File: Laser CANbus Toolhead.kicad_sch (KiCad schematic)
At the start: 79 parts, among them J101 In, J102 Laser, Q101 AO4407A, Q102 2N7002H, U101 STM32F072CBUx, U102 MP2459, U103 XC6206P332MR-G, U104 74AHCT1G125, U105 SN65HVD230, U106 ADXL343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

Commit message: feat: Major hardware upgrade to Rev. 1
- Replace MOSFET with CJAC70P06 (60V voltage rating)
- Upgrade sensor from ADXL345 to ICM-20602 (better availability, 6-axis IMU)
- Change Micro Fit 3.0 connectors from SMD to THT mounting
- Add connector pinouts to silkscreen for easier assembly
- Clean up component placement and optimize layout
- Update overview image to reflect current design
- Add component order numbers to BOM
- Update production files with current components
- Add comprehensive changelog and table of contents
- Improve documentation structure with language links
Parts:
- removed Q101: AO4407A, Package_SO:SOIC-8_3.9x4.9mm_P1.27mm, symbol Transistor_FET:FDS9435A
- removed U106: ADXL343, Package_LGA:LGA-14_3x5mm_P0.8mm_LayoutBorder1x6y, symbol Sensor_Motion:ADXL343
- added C124: 10u, Capacitor_SMD:C_0805_2012Metric, symbol Device:C
- added Q103: CJAC70P06, Package_DFN_QFN:AO_DFN-8-1EP_5.55x5.2mm_P1.27mm_EP4.12x4.6mm, symbol Transistor_FET:AON6411
- added U107: ICM-20602, Package_LGA:LGA-16_3x3mm_P0.5mm_LayoutBorder3x5y, symbol Sensor_Motion:ICM-20602
- C101, C102, C115: LCSC Part # (none) -> C1562; Manufacturer Part # (none) -> 0402CG330J500NT
- C103: value 4u7 -> 10u; footprint Capacitor_SMD:C_0402_1005Metric -> Capacitor_SMD:C_0805_2012Metric; LCSC Part # (none) -> C440198; Manufacturer Part # (none) -> GRM21BR61H106KE43L
- C104: value 4u7 -> 100n; LCSC Part # (none) -> C307331; Manufacturer Part # (none) -> CL05B104KB54PNC
- C105, C106, C107, C108, C109, C111, C113, C114, C117, C118, C120, C122, C123: LCSC Part # (none) -> C307331; Manufacturer Part # (none) -> CL05B104KB54PNC
- C110: value 10uF -> 10u
- C112: value 22uF -> 22u
- C119: LCSC Part # (none) -> C1538; Manufacturer Part # (none) -> 0402B472K500NT
- D103: LCSC Part # (none) -> C343993; Manufacturer Part # (none) -> PESD1CAN
- D104, D105, D106, D107: LCSC Part # (none) -> C2297; Manufacturer Part # (none) -> KT-0805G
- D108: LCSC Part # (none) -> C2296; Manufacturer Part # (none) -> KT-0805Y
- D109, D110: LCSC Part # (none) -> C2286; Manufacturer Part # (none) -> KT-0603R
- J101: footprint Connector_Molex:Molex_Micro-Fit_3.0_43045-0415_2x02_P3.00mm_Vertical -> Connector_Molex:Molex_Micro-Fit_3.0_43045-0412_2x02_P3.00mm_Vertical; FT Rotation Offset (none) -> 180; LCSC Part # (none) -> C492540; Manufacturer Part # (none) -> M3025V-2x2P
- J102: footprint Connector_Molex:Molex_Micro-Fit_3.0_43650-0321_1x03_P3.00mm_Vertical -> Connector_Molex:Molex_Micro-Fit_3.0_43650-0315_1x03_P3.00mm_Vertical; FT Rotation Offset (none) -> 180; LCSC Part # (none) -> C705183; Manufacturer Part # (none) -> M3025V-1x3P
- Q102: value 2N7002H -> 2N7002; LCSC Part # (none) -> C8545; Manufacturer Part # (none) -> 2N7002
- R101, R103, R107, R108, R112, R113: LCSC Part # (none) -> C25744; Manufacturer Part # (none) -> 0402WGF1002TCE
- R102: LCSC Part # (none) -> C25794; Manufacturer Part # (none) -> 0402WGF5102TCE
- R104, R105, R106: LCSC Part # (none) -> C25741; Manufacturer Part # (none) -> 0402WGF1003TCE
- R109, R118: LCSC Part # (none) -> C11702; Manufacturer Part # (none) -> 0402WGF1001TCE
- R110, R111: LCSC Part # (none) -> C60310; Manufacturer Part # (none) -> 0402WGF604JTCE
- R114, R115: LCSC Part # (none) -> C25779; Manufacturer Part # (none) -> 0402WGF3302TCE
- R116: LCSC Part # (none) -> C25890; Manufacturer Part # (none) -> 0402WGF3301TCE
- R117: LCSC Part # (none) -> C25091; Manufacturer Part # (none) -> 0402WGF2200TCE
- R119, R120: LCSC Part # (none) -> C25117; Manufacturer Part # (none) -> 0402WGF4700TCE
- U101: FT Rotation Offset (none) -> 180; LCSC Part # (none) -> C92504; Manufacturer Part # (none) -> STM32F072CBU6
- U102: LCSC Part # (none) -> C39578; Manufacturer Part # (none) -> MP2459GJ-Z
- U103: LCSC Part # (none) -> C5446; Manufacturer Part # (none) -> XC6206P332MR-G
- U104: LCSC Part # (none) -> C7484; Manufacturer Part # (none) -> SN74AHCT1G125DBVR
- U105: LCSC Part # (none) -> C12084; Manufacturer Part # (none) -> SN65HVD230DR
- Y101: LCSC Part # (none) -> C9002; Manufacturer Part # (none) -> X322512MSB4SI
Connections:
- net +24V_{L}: now also Q103.5 (D)
- net GATE_{L}: now also Q103.4 (G)
- net GND: now also C124.2, U107.10 (GND), U107.11 (GND), U107.12 (GND), U107.13 (GND), U107.15 (GND), U107.8 (FSYNC), U107.9 (GND)
- net at D110.2 (A), R107.2: now also U101.26 (PB13); no longer U101.28 (PB15)
- net at R113.1, U101.14 (PA4): now also U107.5 (~{CS})
- net at U101.15 (PA5): now also U107.2 (SCL/SPC)
- net at U101.16 (PA6): now also U107.4 (SAO/SD0)
- net at U101.17 (PA7): now also U107.3 (SDA/SDI)
- net +24V renamed 24V
- net 24V: now also Q103.1 (S), Q103.2 (S), Q103.3 (S)
- net +3.3V renamed 3.3V
- net 3.3V: now also C124.1, U107.1 (VDDIO), U107.16 (VDD); no longer C104.1
- net +5V renamed 5V
- new net: C104.1, U107.14 (REGOUT)
- no-connect marks 4 -> 26
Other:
- company: (none) -> Eduard Iten
- title: (none) -> CANbus Laser Toolhead PCB
- moved on the sheet: C115, C121, C122, C123, R104, R105

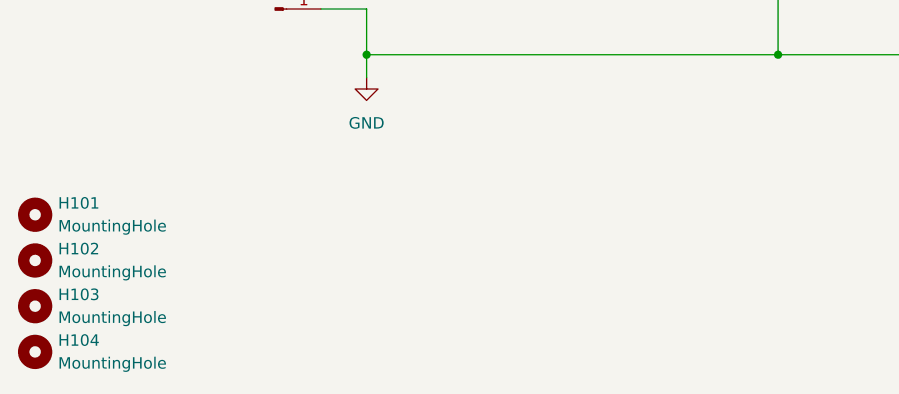
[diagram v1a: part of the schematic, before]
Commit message: docs: Update version numbering to semantic versioning (Rev. 0.0/0.1)
- Rename Rev. 0 to Rev. 0.0 (initial release)
- Rename Rev. 1 to Rev. 0.1 (major hardware upgrade)
- Update all documentation (README and CHANGELOG files)
- Create new git tags with proper semantic versioning
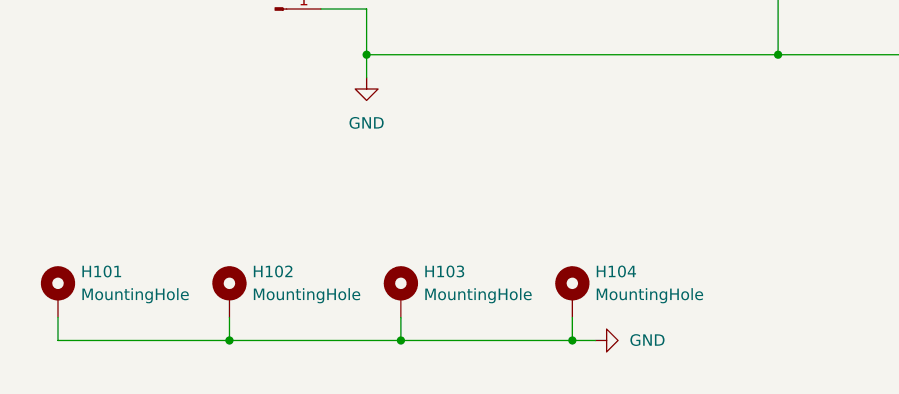
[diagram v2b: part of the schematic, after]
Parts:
- H101, H102, H103, H104: footprint MountingHole:MountingHole_2.7mm_M2.5 -> MountingHole:MountingHole_2.7mm_Pad_Via; symbol Mechanical:MountingHole -> Mechanical:MountingHole_Pad
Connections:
- net GND: now also H101.1, H102.1, H103.1, H104.1

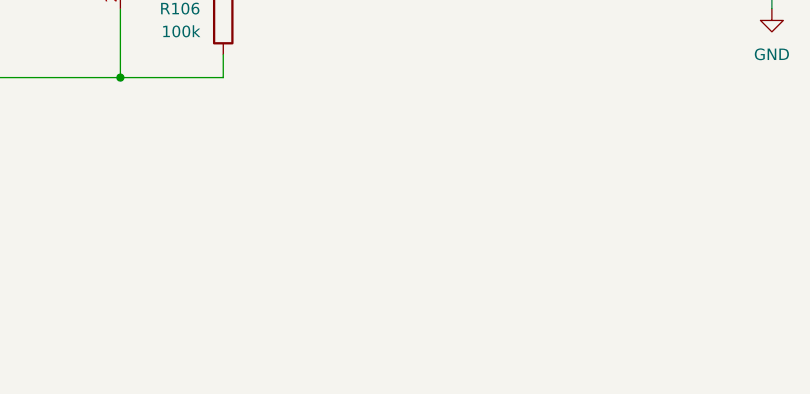
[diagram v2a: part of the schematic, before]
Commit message: feat: Complete project cleanup and Rev. 0.3 updates
- Remove unused schematic files (mcu.kicad_sch, PWR.kicad_sch)
- Update version numbering to semantic versioning (Rev. 0.0/0.1)
- Add comprehensive changelog documentation in both languages
- Create separate CHANGELOG.md and CHANGELOG.de.md files
- Update PCB to Rev. 0.3 with layout optimizations
- Professional 4-layer PCB design with optimal via stitching
- Excellent differential pair routing for CAN-bus (< 18mm)
- Superior thermal management with 19 vias at PFET drain
- Strategic power plane distribution and EMI considerations
- Production-ready PCB layout with best practices implementation
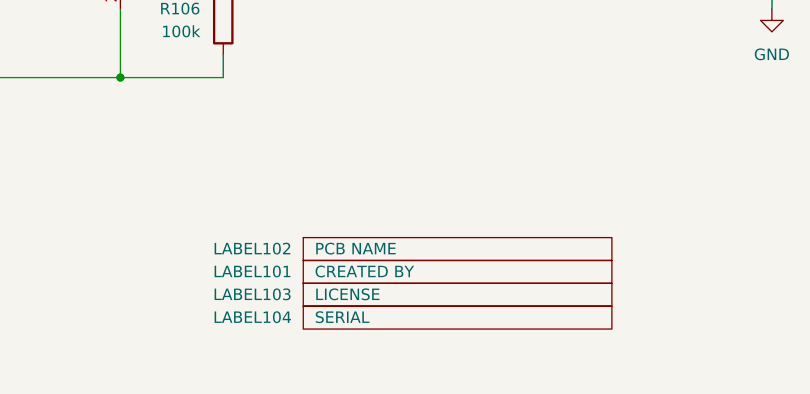
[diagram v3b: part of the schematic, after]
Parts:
- added LABEL101: CREATED BY, prj:EduardIten, symbol prj:LABEL_CREATED_BY
- added LABEL102: PCB NAME, prj:CLT Rev. xxx, symbol prj:LABEL_PCB_NAME
- added LABEL103: LICENSE, prj:CC_BY_NC_SA 4, symbol prj:LABEL_LICENSE
- added LABEL104: SERIAL, prj:SERIAL_No, symbol prj:LABEL_SERIAL
